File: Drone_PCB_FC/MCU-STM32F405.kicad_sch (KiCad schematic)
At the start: 22 parts, among them U4 STM32F405RGTx, Y1 8MHz

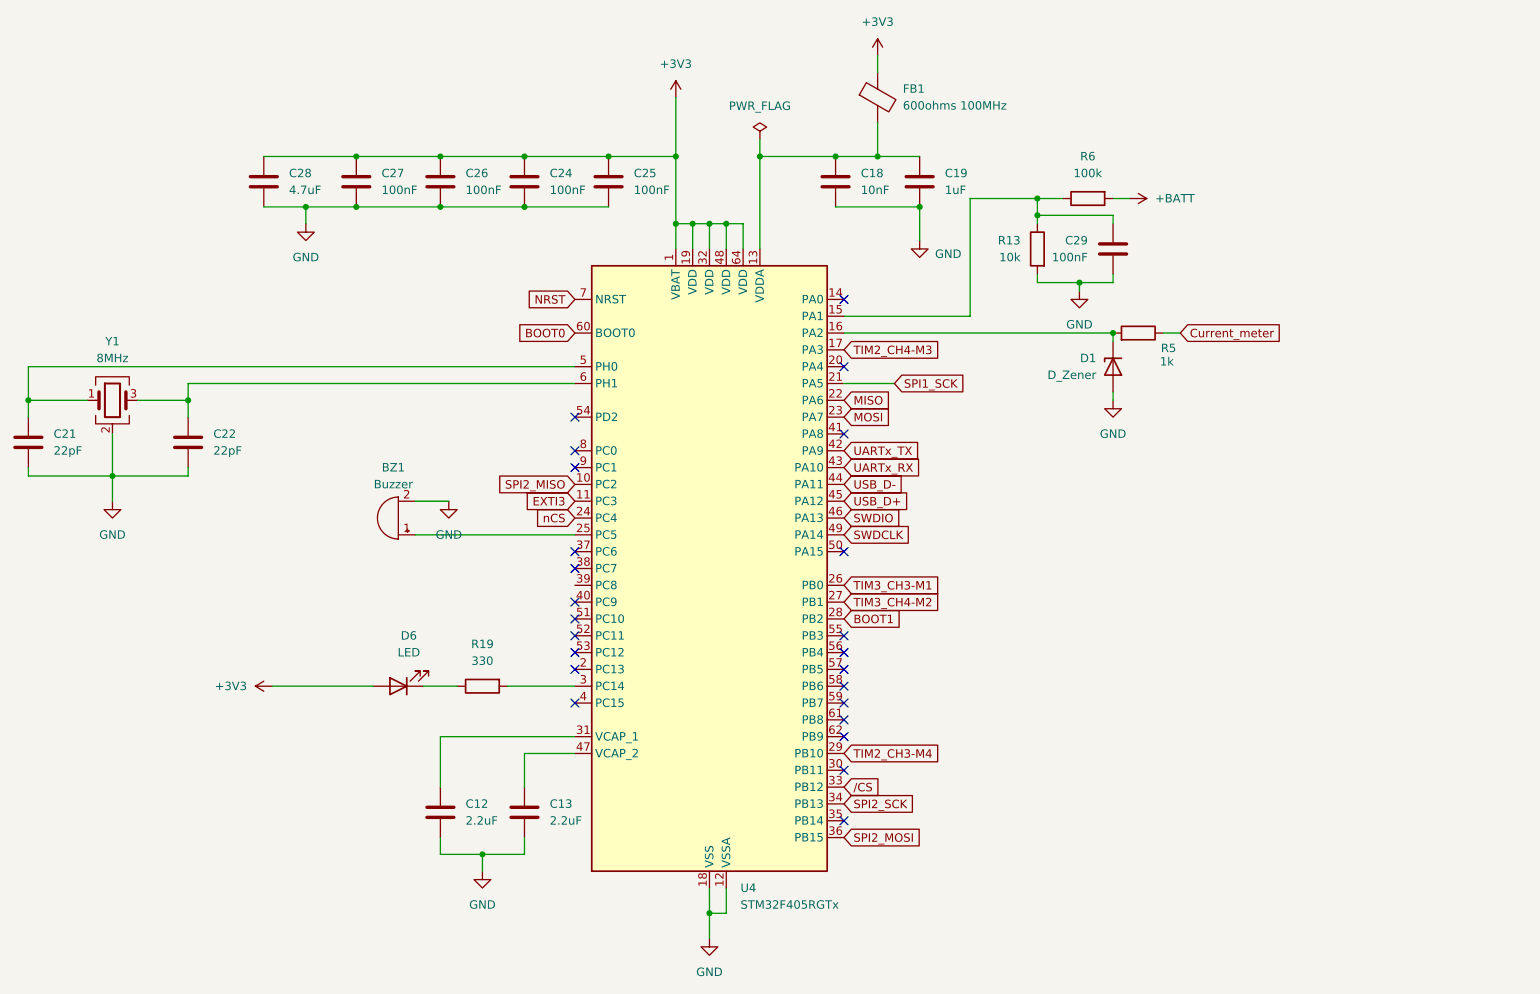
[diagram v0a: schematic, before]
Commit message: 3rd try on the PCB, still need to triple check before I order, and I NEED to check stock because i might need a redesign
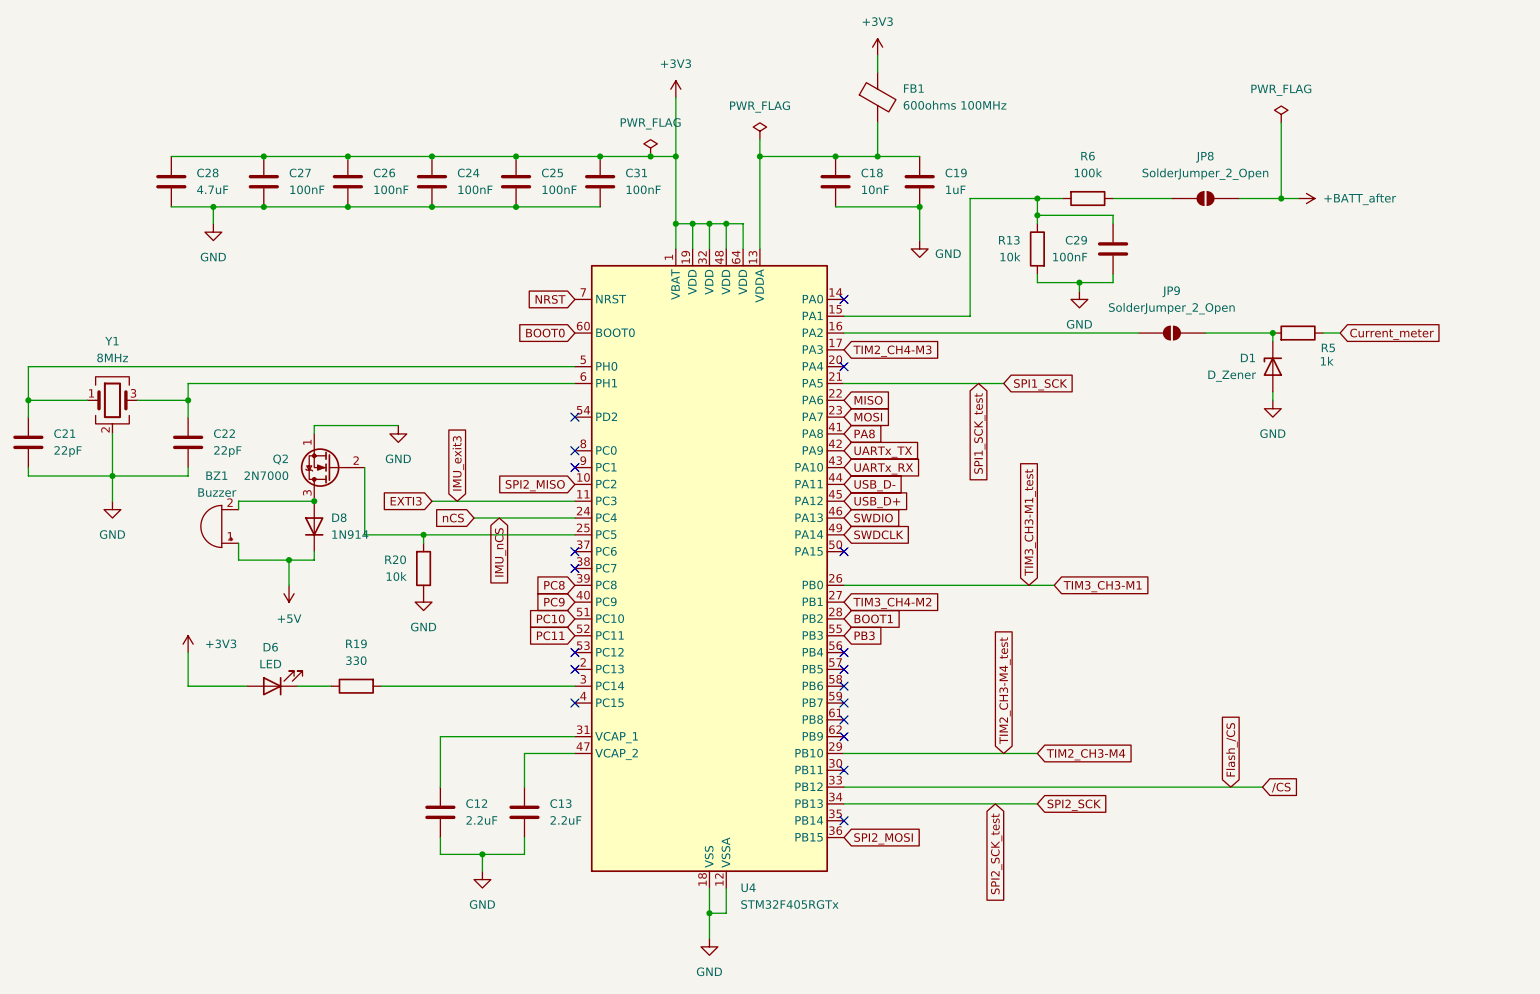
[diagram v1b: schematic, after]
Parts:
- added C31: 100nF, Capacitor_SMD:C_0805_2012Metric, symbol Device:C
- added D8: 1N914, Diode_THT:D_DO-35_SOD27_P7.62mm_Horizontal, symbol Diode:1N914
- added JP8, JP9: SolderJumper_2_Open, Jumper:SolderJumper-2_P1.3mm_Open_RoundedPad1.0x1.5mm, symbol Jumper:SolderJumper_2_Open
- added Q2: 2N7000, Package_TO_SOT_THT:TO-92_Inline, symbol Transistor_FET:2N7000
- added R20: 10k, Resistor_SMD:R_0805_2012Metric, symbol Device:R
- BZ1: footprint (none) -> Buzzer_Beeper:Buzzer_12x9.5RM7.6
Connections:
- net +BATT is gone; now on an unnamed net: R6.2
- net +3V3: now also C31.1
- net GND: now also C31.2, Q2.1 (S), R20.1; no longer BZ1.2 (-)
- net at C29.1, R13.1, U4.15 (PA1): no longer R6.1
- net at D1.1 (K), R5.2: now also JP9.2 (B); no longer U4.16 (PA2)
- net at U4.25 (PC5): now also Q2.2 (G), R20.2; no longer BZ1.1 (+)
- net PC8: now reaches U4.39 (PC8)
- net PC9: now reaches U4.40 (PC9)
- net PA8: now reaches U4.41 (PA8)
- net PC10: now reaches U4.51 (PC10)
- net PC11: now reaches U4.52 (PC11)
- net PB3: now reaches U4.55 (PB3)
- net nCS renamed IMU_nCS
- net /CS renamed Flash_/CS
- new net: BZ1.2 (-), D8.2 (A), Q2.3 (D)
- new net: JP9.1 (A), U4.16 (PA2)
- new net: JP8.1 (A), R6.1
- new net +5V: BZ1.1 (+), D8.1 (K)
- new net +BATT_after: JP8.2 (B)
- no-connect marks 24 -> 19
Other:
- moved on the sheet: BZ1, C24, C25, C26, C27, C28, D1, D6, R19, R5, R6

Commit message: Ordered the PCB now i have to wait and see if i waisted 130 dollars
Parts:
- CurrentM1: renamed from JP9; value SolderJumper_2_Open -> Current M
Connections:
- net +BATT_after: now also R6.1; no longer JP8.2 (B)
- net at C29.1, R13.1, R6.2: now also JP8.1 (A); no longer U4.15 (PA1)
- new net: JP8.2 (B), U4.15 (PA1)
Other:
- moved on the sheet: C29, CurrentM1, D1, JP8, R13, R5, R6
